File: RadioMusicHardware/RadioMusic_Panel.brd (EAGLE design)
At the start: 128.5 x 20 mm, 0 parts

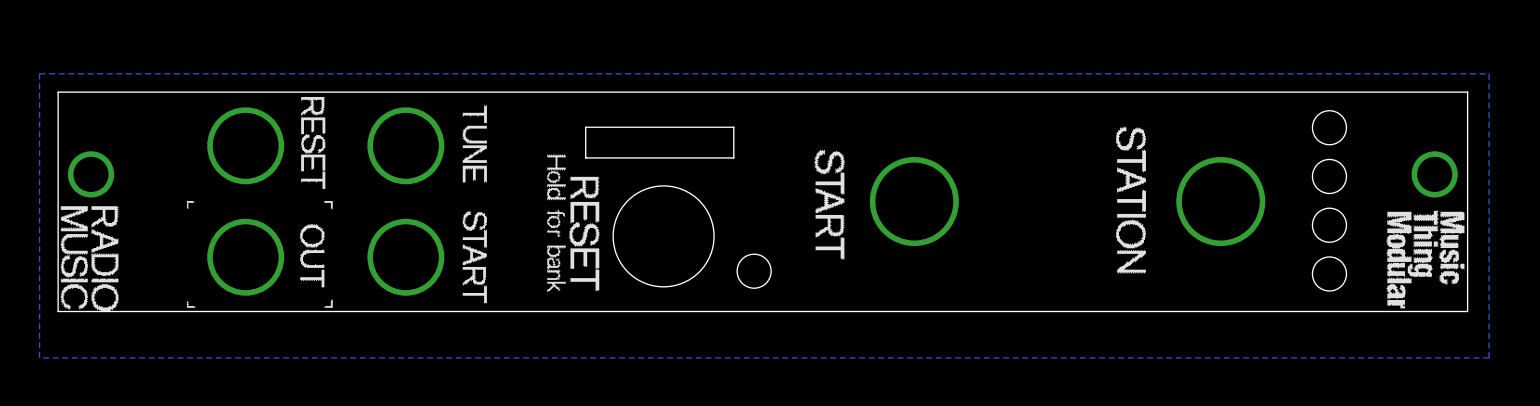
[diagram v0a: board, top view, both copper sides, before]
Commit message: Front panel cosmetic fixes
Fixes #19
Fixes #18
Fixes #17
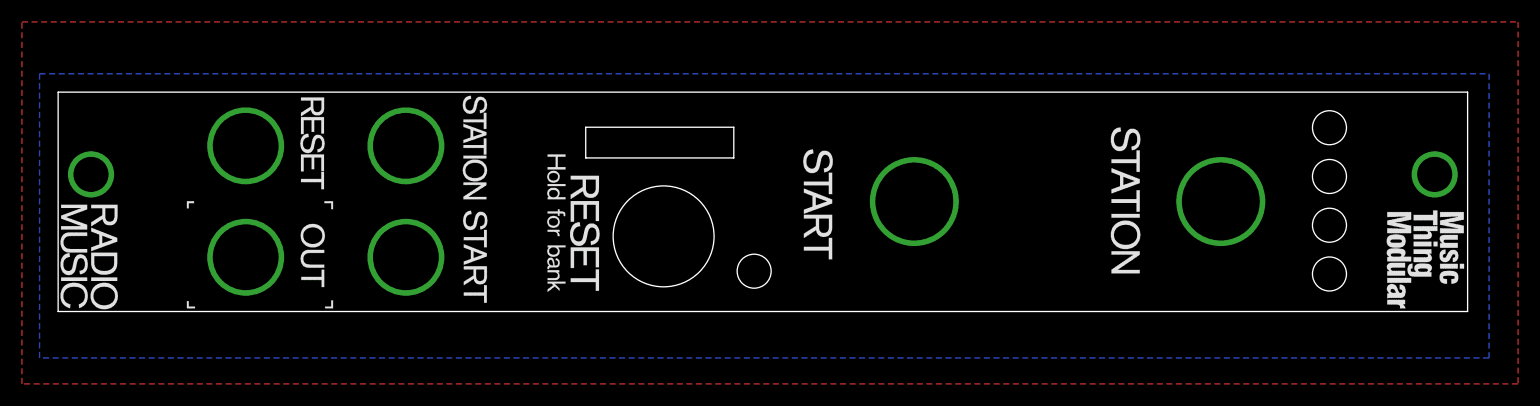
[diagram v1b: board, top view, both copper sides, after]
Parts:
- added U$1: (no value), TW_logos:MTM_2CM
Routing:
- added copper zone on layer 1, net GND
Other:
- board text added: "RadioMusic Panel PCB rev 2 Designed in Herne Hill, London by Tom Whitwell December 2014 CC-BY-SA musicthing.co.uk"
- board text removed: "RadioMusic Panel PCB rev 1 Designed in Herne Hill, London by Tom Whitwell October 2014 CC-BY-SA musicthing.co.uk"
